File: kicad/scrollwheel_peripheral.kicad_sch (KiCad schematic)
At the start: 9 parts, among them J1 Conn_01x14_Socket, J2 Conn_01x14_Socket, J3 Conn_01x05_Socket

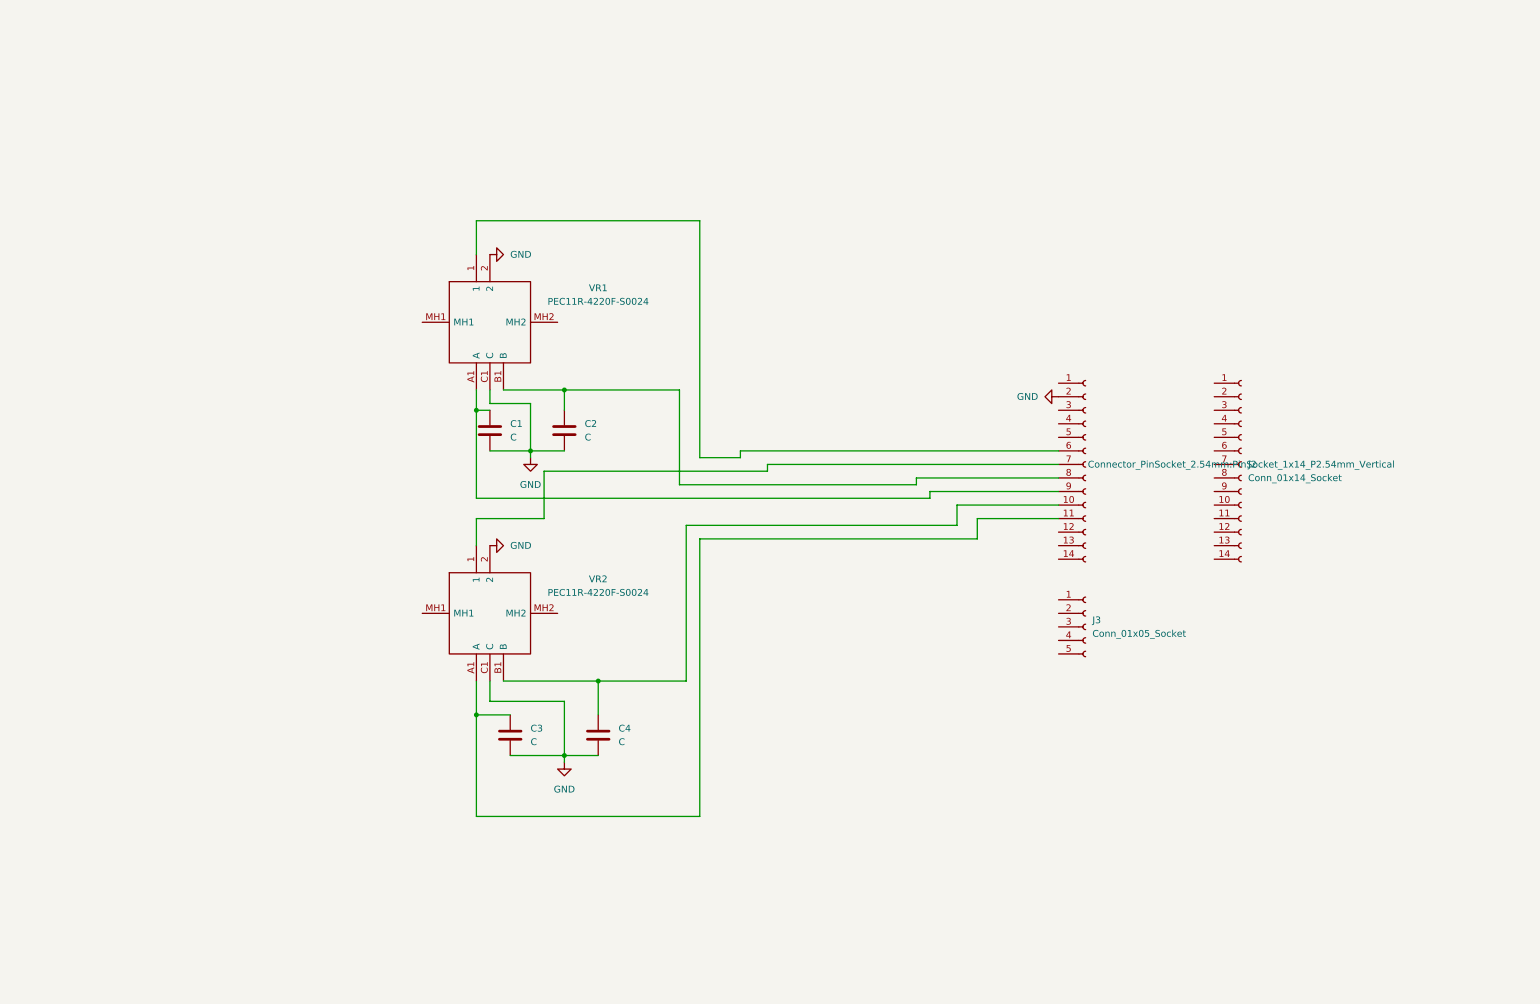
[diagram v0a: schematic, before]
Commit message: Schematic with Atmega
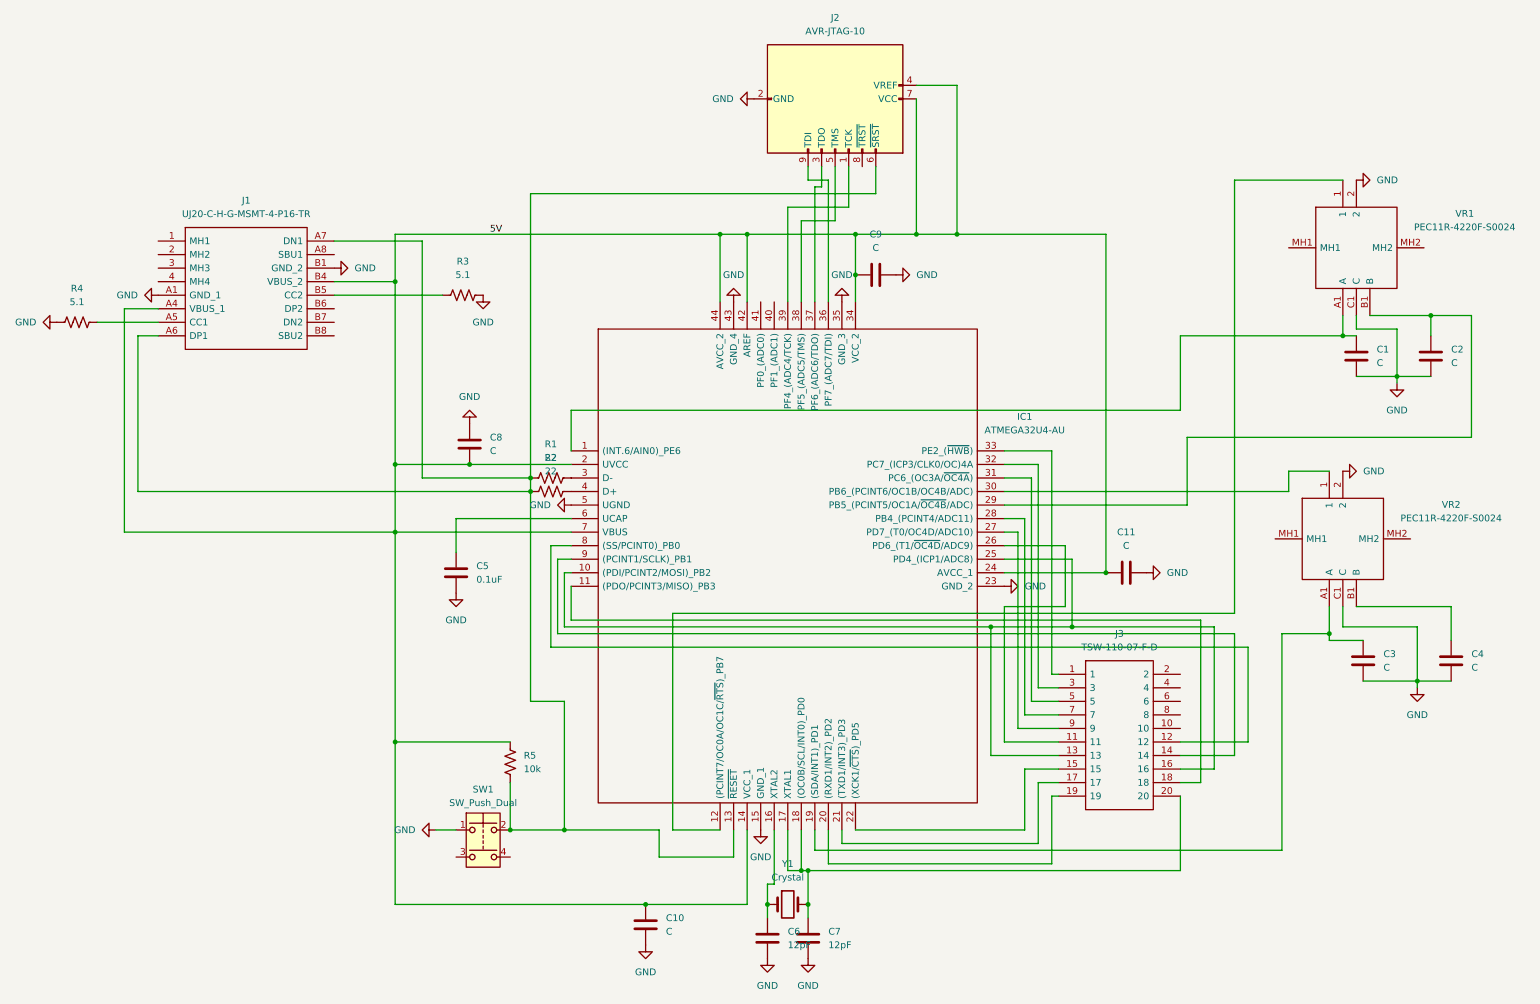
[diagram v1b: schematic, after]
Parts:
- removed J1, J2: Conn_01x14_Socket, Connector_PinSocket_2.54mm:PinSocket_1x14_P2.54mm_Vertical, symbol Connector:Conn_01x14_Socket
- removed J3: Conn_01x05_Socket, Connector_PinSocket_2.54mm:PinSocket_1x05_P2.54mm_Vertical, symbol Connector:Conn_01x05_Socket
- added C10, C11, C8, C9: C, symbol Device:C
- added C5: 0.1uF, symbol Device:C
- added C6, C7: 12pF, symbol Device:C
- added IC1: ATMEGA32U4-AU, QFP80P1200X1200X120-44N, symbol ATMEGA32U4-AU:ATMEGA32U4-AU
- added J1: UJ20-C-H-G-MSMT-4-P16-TR, UJ20CHGMSMT4P16TR, symbol UJ20-C-H-G-MSMT-4-P16-TR:UJ20-C-H-G-MSMT-4-P16-TR
- added J2: AVR-JTAG-10, symbol Connector:AVR-JTAG-10
- added J3: TSW-110-07-F-D, TSW-110-XX-YY-D, symbol TSW-110-07-F-D:TSW-110-07-F-D
- added R1, R2: 22, symbol Device:R_US
- added R3, R4: 5.1, symbol Device:R_US
- added R5: 10k, symbol Device:R_US
- added SW1: SW_Push_Dual, symbol Switch:SW_Push_Dual
- added Y1: Crystal, symbol Device:Crystal
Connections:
- net GND: now also C10.2, C11.2, C5.2, C6.2, C7.2, C8.1, C9.2, IC1.15 (GND_1), IC1.23 (GND_2), IC1.35 (GND_3), IC1.43 (GND_4), IC1.5 (UGND), J1.A1 (GND_1), J1.B1 (GND_2), J2.10 (GND), J2.2 (GND), R3.2, R4.1, SW1.1
- net at C2.1, VR1.B1 (B): now also IC1.29 (PB5_(PCINT5/OC1A/~{OC4B}/ADC))
- net at VR1.1: now also IC1.12 ((PCINT7/OC0A/OC1C/~{RTS})_PB7)
- net at C1.1, VR1.A1 (A): now also IC1.1 ((INT.6/AIN0)_PE6)
- net at VR2.1: now also IC1.30 (PB6_(PCINT6/OC1B/OC4B/ADC))
- net at C3.1, VR2.A1 (A): now also IC1.19 ((SDA/INT1)_PD1)
- new net: J1.A5 (CC1), R4.2
- new net: IC1.13 (~{RESET}), J1.A6 (DP1), J1.A7 (DN1), J2.6 (~{SRST}), R1.1, R2.1, R5.2, SW1.2
- new net: J1.B5 (CC2), R3.1
- new net: C7.1, IC1.17 (XTAL1), IC1.18 ((OC0B/SCL/INT0)_PD0), J3.20, Y1.2
- new net: C6.1, IC1.16 (XTAL2), Y1.1
- new net: IC1.3 (D-), R1.2
- new net: IC1.39 (PF4_(ADC4/TCK)), J2.1 (TCK)
- new net: IC1.37 (PF6_(ADC6/TDO)), J2.3 (TDO)
- new net: IC1.38 (PF5_(ADC5/TMS)), J2.5 (TMS)
- new net: IC1.36 (PF7_(ADC7/TDI)), J2.9 (TDI)
- new net: IC1.33 (PE2_(~{HWB})), J3.1
- new net: IC1.26 (PD6_(T1/~{OC4D}/ADC9)), J3.11
- new net: IC1.8 ((SS/PCINT0)_PB0), J3.12
- new net: IC1.10 ((PDI/PCINT2/MOSI)_PB2), IC1.25 (PD4_(ICP1/ADC8)), J3.13, J3.16
- new net: IC1.9 ((PCINT1/SCLK)_PB1), J3.14
- new net: IC1.22 ((XCK1/~{CTS})_PD5), J3.15
- new net: IC1.21 ((TXD1/INT3)_PD3), J3.17
- new net: IC1.11 ((PDO/PCINT3/MISO)_PB3), J3.18
- new net: IC1.20 ((RXD1/INT2)_PD2), J3.19
- new net: IC1.32 (PC7_(ICP3/CLK0/OC)4A), J3.3
- new net: IC1.31 (PC6_(OC3A/~{OC4A})), J3.5
- new net: IC1.28 (PB4_(PCINT4/ADC11)), J3.7
- new net: IC1.27 (PD7_(T0/OC4D/ADC10)), J3.9
- new net: IC1.4 (D+), R2.2
- new net: C5.1, IC1.6 (UCAP)
- new net 5V: C10.1, C11.1, C8.2, C9.1, IC1.14 (VCC_1), IC1.2 (UVCC), IC1.24 (AVCC_1), IC1.34 (VCC_2), IC1.42 (AREF), IC1.44 (AVCC_2), IC1.7 (VBUS), J1.A4 (VBUS_1), J1.B4 (VBUS_2), J2.4 (VREF), J2.7 (VCC), R5.1
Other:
- moved on the sheet: C1, C2, C3, C4, VR1, VR2

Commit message: footprints
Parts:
- C10, C11, C5, C6, C7, C8, C9: footprint (none) -> Capacitor_SMD:C_0805_2012Metric
- IC1: footprint QFP80P1200X1200X120-44N -> project_footprints:QFP80P1200X1200X120-44N
- J1: footprint UJ20CHGMSMT4P16TR -> project_footprints:UJ20CHGMSMT4P16TR
- J2: footprint (none) -> project_footprints:TSW-110-XX-YY-D
- J3: footprint TSW-110-XX-YY-D -> project_footprints:TSW-110-XX-YY-D
- R1, R2, R3, R4, R5: footprint (none) -> Resistor_SMD:R_0805_2012Metric
- SW1: footprint (none) -> Button_Switch_SMD:SW_DIP_SPSTx02_Slide_9.78x7.26mm_W8.61mm_P2.54mm
- VR1, VR2: footprint PEC11R4220FS0024 -> project_footprints:PEC11R4220FS0024
- Y1: footprint (none) -> Crystal:Crystal_DS26_D2.0mm_L6.0mm_Horizontal
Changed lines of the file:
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@@
 			)
 		)
-		(property "Footprint" "UJ20CHGMSMT4P16TR"
+		(property "Footprint" "project_footprints:UJ20CHGMSMT4P16TR"
 			(at 49.53 40.64 0)
 			(effects
@@
 			)
 		)
-		(property "Footprint" ""
+		(property "Footprint" "Resistor_SMD:R_0805_2012Metric"
 			(at 77.724 52.324 90)
 			(effects
@@
 			)
 		)
-		(property "Footprint" ""
+		(property "Footprint" "Resistor_SMD:R_0805_2012Metric"
 			(at 5.334 57.404 90)
 			(effects
@@
 			)
 		)
-		(property "Footprint" ""
+		(property "Footprint" "Capacitor_SMD:C_0805_2012Metric"
 			(at 143.2052 177.8 0)
 			(effects
@@
 			)
 		)
-		(property "Footprint" "PEC11R4220FS0024"
+		(property "Footprint" "project_footprints:PEC11R4220FS0024"
 			(at 254 36.83 0)
 			(effects
@@
 			)
 		)
-		(property "Footprint" ""
+		(property "Footprint" "Capacitor_SMD:C_0805_2012Metric"
 			(at 112.7252 175.26 0)
 			(effects
@@
 			)
 		)
-		(property "Footprint" ""
+		(property "Footprint" "Capacitor_SMD:C_0805_2012Metric"
 			(at 135.5852 177.8 0)
 			(effects
@@
 			)
 		)
-		(property "Footprint" "PEC11R4220FS0024"
+		(property "Footprint" "project_footprints:PEC11R4220FS0024"
 			(at 251.46 91.44 0)
 			(effects
@@
 			)
 		)
-		(property "Footprint" ""
+		(property "Footprint" "Crystal:Crystal_DS26_D2.0mm_L6.0mm_Horizontal"
 			(at 138.43 167.64 0)
 			(effects
@@
 			)
 		)
-		(property "Footprint" ""
+		(property "Footprint" "Resistor_SMD:R_0805_2012Metric"
 			(at 94.234 86.614 90)
 			(effects
@@
 			)
 		)
-		(property "Footprint" ""
+		(property "Footprint" "Capacitor_SMD:C_0805_2012Metric"
 			(at 158.75 48.5648 0)
 			(effects
@@
 			)
 		)
-		(property "Footprint" ""
+		(property "Footprint" "project_footprints:TSW-110-XX-YY-D"
 			(at 151.13 12.7 90)
 			(effects
@@
 			)
 		)
-		(property "Footprint" ""
+		(property "Footprint" "Capacitor_SMD:C_0805_2012Metric"
 			(at 79.7052 85.09 0)
 			(effects
@@
 			)
 		)
-		(property "Footprint" "TSW-110-XX-YY-D"
+		(property "Footprint" "project_footprints:TSW-110-XX-YY-D"
 			(at 208.28 121.92 0)
 			(effects
@@
 			)
 		)
-		(property "Footprint" "QFP80P1200X1200X120-44N"
+		(property "Footprint" "project_footprints:QFP80P1200X1200X120-44N"
 			(at 175.26 59.69 0)
 			(effects
@@
 			)
 		)
-		(property "Footprint" ""
+		(property "Footprint" "Resistor_SMD:R_0805_2012Metric"
 			(at 94.234 89.154 90)
 			(effects
@@
 			)
 		)
-		(property "Footprint" ""
+		(property "Footprint" "Button_Switch_SMD:SW_DIP_SPSTx02_Slide_9.78x7.26mm_W8.61mm_P2.54mm"
 			(at 81.28 148.59 0)
 			(effects
@@
 			)
 		)
-		(property "Footprint" ""
+		(property "Footprint" "Capacitor_SMD:C_0805_2012Metric"
 			(at 77.1652 109.22 0)
 			(effects
@@
 			)
 		)
-		(property "Footprint" ""
+		(property "Footprint" "Capacitor_SMD:C_0805_2012Metric"
 			(at 205.74 104.4448 0)
 			(effects
@@
 			)
 		)
-		(property "Footprint" ""
+		(property "Footprint" "Resistor_SMD:R_0805_2012Metric"
 			(at 87.376 141.224 90)
 			(effects

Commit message: Part selection; Board
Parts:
- C6, C7: value 12pF -> 22pF
- J2: footprint project_footprints:TSW-110-XX-YY-D -> Connector_PinHeader_2.54mm:PinHeader_2x05_P2.54mm_Vertical
- SW1: footprint Button_Switch_SMD:SW_DIP_SPSTx02_Slide_9.78x7.26mm_W8.61mm_P2.54mm -> Button_Switch_THT:SW_PUSH_6mm
- Y1: footprint Crystal:Crystal_DS26_D2.0mm_L6.0mm_Horizontal -> Crystal:Crystal_SMD_Abracon_ABM3-2Pin_5.0x3.2mm
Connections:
- net at IC1.13 (~{RESET}), J2.6 (~{SRST}), R5.2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: no longer J1.A6 (DP1), J1.A7 (DN1), R1.1, R2.1
- net at C7.1, IC1.17 (XTAL1), Y1.2: no longer IC1.18 ((OC0B/SCL/INT0)_PD0), J3.20
- new net: J1.A6 (DP1), R2.1
- new net: J1.A7 (DN1), R1.1
- new net: IC1.18 ((OC0B/SCL/INT0)_PD0), J3.20
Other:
- moved on the sheet: R1, R2
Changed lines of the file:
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@@
 	)
 	(junction
-		(at 90.17 87.63)
-		(diameter 0)
-		(color 0 0 0 0)
-	)
-	(junction
 		(at 134.62 167.64)
 		(diameter 0)
@@
 	)
 	(junction
-		(at 142.24 161.29)
-		(diameter 0)
-		(color 0 0 0 0)
-	)
-	(junction
 		(at 242.57 60.96)
 		(diameter 0)
@@
 	)
 	(junction
-		(at 140.97 161.29)
-		(diameter 0)
-		(color 0 0 0 0)
-	)
-	(junction
 		(at 191.77 115.57)
 		(diameter 0)
@@
 	)
 	(junction
-		(at 90.17 90.17)
-		(diameter 0)
-		(color 0 0 0 0)
-	)
-	(junction
 		(at 151.13 49.53)
 		(diameter 0)
@@
 	(wire
 		(pts
-			(xy 90.17 90.17) (xy 90.17 129.54)
-		)
-		(stroke
-			(width 0)
-			(type default)
-		)
-	)
-	(wire
-		(pts
 			(xy 135.89 163.83) (xy 134.62 163.83)
 		)
@@
 	(wire
 		(pts
-			(xy 252.73 68.58) (xy 259.08 68.58)
+			(xy 140.97 160.02) (xy 144.78 160.02)
 		)
 		(stroke
@@
 	(wire
 		(pts
-			(xy 90.17 129.54) (xy 96.52 129.54)
+			(xy 252.73 68.58) (xy 259.08 68.58)
 		)
 		(stroke
@@
 	(wire
 		(pts
-			(xy 218.44 142.24) (xy 218.44 115.57)
+			(xy 90.17 129.54) (xy 96.52 129.54)
 		)
 		(stroke
@@
 	(wire
 		(pts
-			(xy 142.24 170.18) (xy 142.24 167.64)
+			(xy 218.44 142.24) (xy 218.44 115.57)
 		)
 		(stroke
@@
 	(wire
 		(pts
-			(xy 242.57 115.57) (xy 256.54 115.57)
+			(xy 142.24 170.18) (xy 142.24 167.64)
 		)
 		(stroke
@@
 	(wire
 		(pts
-			(xy 90.17 87.63) (xy 90.17 90.17)
+			(xy 242.57 115.57) (xy 256.54 115.57)
 		)
 		(stroke
@@
 	(wire
 		(pts
-			(xy 130.81 41.91) (xy 130.81 54.61)
+			(xy 90.17 34.29) (xy 90.17 129.54)
 		)
 		(stroke
@@
 	(wire
 		(pts
-			(xy 142.24 161.29) (xy 212.09 161.29)
+			(xy 130.81 41.91) (xy 130.81 54.61)
 		)
 		(stroke
@@
 	(wire
 		(pts
-			(xy 16.51 90.17) (xy 90.17 90.17)
+			(xy 151.13 153.67) (xy 182.88 153.67)
 		)
 		(stroke
@@
 	(wire
 		(pts
-			(xy 151.13 153.67) (xy 182.88 153.67)
+			(xy 240.03 118.11) (xy 246.38 118.11)
 		)
 		(stroke
@@
 	(wire
 		(pts
-			(xy 240.03 118.11) (xy 246.38 118.11)
+			(xy 97.79 82.55) (xy 97.79 74.93)
 		)
 		(stroke
@@
 	(wire
 		(pts
-			(xy 97.79 82.55) (xy 97.79 74.93)
+			(xy 142.24 161.29) (xy 142.24 167.64)
 		)
 		(stroke
@@
 	(wire
 		(pts
+			(xy 87.63 87.63) (xy 97.79 87.63)
+		)
+		(stroke
+			(width 0)
+			(type default)
+		)
+	)
+	(wire
+		(pts
 			(xy 198.12 105.41) (xy 198.12 41.91)
 		)
@@
 	(wire
 		(pts
+			(xy 87.63 90.17) (xy 97.79 90.17)
+		)
+		(stroke
+			(width 0)
+			(type default)
+		)
+	)
+	(wire
+		(pts
 			(xy 181.61 97.79) (xy 181.61 134.62)
 		)
@@
 	(wire
 		(pts
-			(xy 142.24 161.29) (xy 142.24 167.64)
+			(xy 16.51 90.17) (xy 80.01 90.17)
 		)
 		(stroke
@@
 	(wire
 		(pts
-			(xy 78.74 85.09) (xy 97.79 85.09)
+			(xy 69.85 87.63) (xy 80.01 87.63)
 		)
 		(stroke
@@
 	(wire
 		(pts
-			(xy 151.13 41.91) (xy 130.81 41.91)
+			(xy 78.74 85.09) (xy 97.79 85.09)
 		)
 		(stroke
@@
 	(wire
 		(pts
-			(xy 212.09 137.16) (xy 224.79 137.16)
+			(xy 151.13 41.91) (xy 130.81 41.91)
 		)
 		(stroke
@@
 	(wire
 		(pts
-			(xy 146.05 160.02) (xy 187.96 160.02)
+			(xy 212.09 137.16) (xy 224.79 137.16)
 		)
 		(stroke
@@
 	(wire
 		(pts
-			(xy 182.88 142.24) (xy 189.23 142.24)
+			(xy 146.05 160.02) (xy 187.96 160.02)
 		)
 		(stroke
@@
 	(wire
 		(pts
-			(xy 140.97 161.29) (xy 142.24 161.29)
+			(xy 182.88 142.24) (xy 189.23 142.24)
 		)
 		(stroke
@@
 	(wire
 		(pts
-			(xy 138.43 161.29) (xy 140.97 161.29)
-		)
-		(stroke
-			(width 0)
-			(type default)
-		)
-	)
-	(wire
-		(pts
 			(xy 170.18 13.97) (xy 170.18 41.91)
 		)
@@
 	(wire
 		(pts
-			(xy 140.97 153.67) (xy 140.97 161.29)
-		)
-		(stroke
-			(width 0)
-			(type default)
-		)
-	)
-	(wire
-		(pts
 			(xy 190.5 111.76) (xy 179.07 111.76)
 		)
@@
 	(wire
 		(pts
-			(xy 69.85 87.63) (xy 90.17 87.63)
+			(xy 259.08 57.15) (xy 259.08 60.96)
 		)
 		(stroke
@@
 	(wire
 		(pts
-			(xy 259.08 57.15) (xy 259.08 60.96)
+			(xy 140.97 54.61) (xy 140.97 39.37)
 		)
 		(stroke
@@
 	(wire
 		(pts
-			(xy 140.97 54.61) (xy 140.97 39.37)
+			(xy 185.42 85.09) (xy 185.42 127)
 		)
 		(stroke
@@
 	(wire
 		(pts
-			(xy 185.42 85.09) (xy 185.42 127)
+			(xy 116.84 113.03) (xy 222.25 113.03)
 		)
 		(stroke
@@
 	(wire
 		(pts
-			(xy 116.84 113.03) (xy 222.25 113.03)
+			(xy 144.78 160.02) (xy 144.78 162.56)
 		)
 		(stroke
@@
 	(wire
 		(pts
+			(xy 138.43 161.29) (xy 142.24 161.29)
+		)
+		(stroke
+			(width 0)
+			(type default)
+		)
+	)
+	(wire
+		(pts
 			(xy 187.96 160.02) (xy 187.96 147.32)
 		)
@@
 	(wire
 		(pts
+			(xy 212.09 147.32) (xy 212.09 162.56)
+		)
+		(stroke
+			(width 0)
+			(type default)
+		)
+	)
+	(wire
+		(pts
 			(xy 20.32 55.88) (xy 13.97 55.88)
 		)
@@
 	(wire
 		(pts
-			(xy 179.07 137.16) (xy 189.23 137.16)
+			(xy 140.97 153.67) (xy 140.97 160.02)
 		)
 		(stroke
@@
 	(wire
 		(pts
-			(xy 198.12 41.91) (xy 170.18 41.91)
+			(xy 179.07 137.16) (xy 189.23 137.16)
 		)
 		(stroke
@@
 	(wire
 		(pts
-			(xy 212.09 161.29) (xy 212.09 147.32)
+			(xy 198.12 41.91) (xy 170.18 41.91)
 		)
 		(stroke
@@
 	(wire
 		(pts
+			(xy 144.78 162.56) (xy 212.09 162.56)
+		)
+		(stroke
+			(width 0)
+			(type default)
+		)
+	)
+	(wire
+		(pts
 			(xy 95.25 102.87) (xy 97.79 102.87)
 		)
@@
 	(wire
 		(pts
-			(xy 90.17 34.29) (xy 90.17 87.63)
-		)
-		(stroke
-			(width 0)
-			(type default)
-		)
-	)
-	(wire
-		(pts
 			(xy 97.79 95.25) (xy 76.2 95.25)
 		)
@@
 			)
 		)
-		(property "Value" "12pF"
+		(property "Value" "22pF"
 			(at 146.05 175.2599 0)
 			(effects
@@
 			)
 		)
-		(property "Value" "12pF"
+		(property "Value" "22pF"
 			(at 138.43 175.2599 0)
 			(effects
@@
 			)
 		)
-		(property "Footprint" "Crystal:Crystal_DS26_D2.0mm_L6.0mm_Horizontal"
+		(property "Footprint" "Crystal:Crystal_SMD_Abracon_ABM3-2Pin_5.0x3.2mm"
 			(at 138.43 167.64 0)
 			(effects
@@
 	(symbol
 		(lib_id "Device:R_US")
-		(at 93.98 87.63 90)
+		(at 83.82 87.63 90)
 		(unit 1)
 		(exclude_from_sim no)
@@
 		(fields_autoplaced yes)
 		(property "Reference" "R1"
-			(at 93.98 81.28 90)
+			(at 83.82 81.28 90)
 			(effects
 				(font
@@
 		)
 		(property "Value" "22"
-			(at 93.98 83.82 90)
+			(at 83.82 83.82 90)
 			(effects
 				(font
@@
 		)
 		(property "Footprint" "Resistor_SMD:R_0805_2012Metric"
-			(at 94.234 86.614 90)
+			(at 84.074 86.614 90)
 			(effects
 				(font
@@
 		)
 		(property "Datasheet" "~"
-			(at 93.98 87.63 0)
+			(at 83.82 87.63 0)
 			(effects
 				(font
@@
 		)
 		(property "Description" "Resistor, US symbol"
-			(at 93.98 87.63 0)
+			(at 83.82 87.63 0)
 			(effects
 				(font
@@
 			)
 		)
-		(property "Footprint" "project_footprints:TSW-110-XX-YY-D"
+		(property "Footprint" "Connector_PinHeader_2.54mm:PinHeader_2x05_P2.54mm_Vertical"
 			(at 151.13 12.7 90)
 			(effects
@@
 	(symbol
 		(lib_id "Device:R_US")
-		(at 93.98 90.17 90)
+		(at 83.82 90.17 90)
 		(unit 1)
 		(exclude_from_sim no)
@@
 		(fields_autoplaced yes)
 		(property "Reference" "R2"
-			(at 93.98 83.82 90)
+			(at 83.82 83.82 90)
 			(effects
 				(font
@@
 		)
 		(property "Value" "22"
-			(at 93.98 86.36 90)
+			(at 83.82 86.36 90)
 			(effects
 				(font
@@
 		)
 		(property "Footprint" "Resistor_SMD:R_0805_2012Metric"
-			(at 94.234 89.154 90)
+			(at 84.074 89.154 90)
 			(effects
 				(font
@@
 		)
 		(property "Datasheet" "~"
-			(at 93.98 90.17 0)
+			(at 83.82 90.17 0)
 			(effects
 				(font
@@
 		)
 		(property "Description" "Resistor, US symbol"
-			(at 93.98 90.17 0)
+			(at 83.82 90.17 0)
 			(effects
 				(font
@@
 			)
 		)
-		(property "Footprint" "Button_Switch_SMD:SW_DIP_SPSTx02_Slide_9.78x7.26mm_W8.61mm_P2.54mm"
+		(property "Footprint" "Button_Switch_THT:SW_PUSH_6mm"
 			(at 81.28 148.59 0)
 			(effects

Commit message: Finish routing for rev 1
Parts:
- removed J3: TSW-110-07-F-D, project_footprints:TSW-110-XX-YY-D, symbol TSW-110-07-F-D:TSW-110-07-F-D
- removed SW1: SW_Push_Dual, Button_Switch_THT:SW_PUSH_6mm, symbol Switch:SW_Push_Dual
- added SW2: SW_Push, Button_Switch_THT:SW_PUSH_6mm, symbol Switch:SW_Push
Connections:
- net GND: now also SW2.1
- net at C2.1, VR1.B1 (B): now also IC1.30 (PB6_(PCINT6/OC1B/OC4B/ADC)); no longer IC1.29 (PB5_(PCINT5/OC1A/~{OC4B}/ADC))
- net at VR1.1: now also IC1.28 (PB4_(PCINT4/ADC11)); no longer IC1.12 ((PCINT7/OC0A/OC1C/~{RTS})_PB7)
- net at C1.1, VR1.A1 (A): now also IC1.29 (PB5_(PCINT5/OC1A/~{OC4B}/ADC)); no longer IC1.1 ((INT.6/AIN0)_PE6)
- net at VR2.1: now also IC1.10 ((PDI/PCINT2/MOSI)_PB2); no longer IC1.30 (PB6_(PCINT6/OC1B/OC4B/ADC))
- net at C3.1, VR2.A1 (A): now also IC1.8 ((SS/PCINT0)_PB0); no longer IC1.19 ((SDA/INT1)_PD1)
- net at C4.1, VR2.B1 (B): now also IC1.9 ((PCINT1/SCLK)_PB1)
- net at IC1.13 (~{RESET}), J2.6 (~{SRST}), R5.2: now also SW2.2
- net at IC1.25 (PD4_(ICP1/ADC8)): no longer IC1.10 ((PDI/PCINT2/MOSI)_PB2)
